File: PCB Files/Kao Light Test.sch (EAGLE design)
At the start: 12 parts, among them Q1 MMBT3904-TP

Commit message: feat: updates PCB
Adds changes from Issue #9
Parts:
- removed BT1, BT2, BT3: BHX1-1025-SM, BHX1-1025-SM:BHX1-1025-SM
- removed Q1: MMBT3904-TP, MMBT3904-TP:MMBT3904-TP
- added ANALOG: (no value), SparkFun-Connectors:JST_2MM_MALE
- added CN1: (no value), adafruit:JST_2PIN-THM
- added R10, R11, R12, R13, R14, R3, R4, R5, R6, R7, R8, R9: 1k, SparkFun-Resistors:1KOHM-HORIZ-1/4W-1%
- added T1: 2N2222, adafruit:2N2222
- R2: device SparkFun-Resistors:10KOHM-HORIZ-1/4W-1% -> SparkFun-Resistors:330OHM-HORIZ-1/10W-5%
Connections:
- removed net GND_2: DIGITAL-OUT.13, U$1.GND1
- removed net GND_3: BT3.-, DIGITAL-OUT.1
- removed net N$17: BT2.-, BT3.+
- removed net N$4: Q1.3, R2.1
- new net D14: ANALOG.+, DIGITAL-OUT.17
- net D1: now also R14.2
- net D10: now also R5.2
- net D11: now also R4.2
- net D12: now also R3.2
- net D2: now also R13.2
- net D3: now also R12.2
- net D4: now also R11.2
- net D5: now also R10.2
- net D6: now also R9.2
- net D7: now also R8.2
- net D8: now also R7.2
- net D9: now also R6.2
- net GND_1: now also ANALOG.-, CN1.1, DIGITAL-OUT.13, R10.1, R11.1, R12.1, R13.1, R14.1, R3.1, R4.1, R5.1, R6.1, R7.1, R8.1, R9.1, T1.E, U$1.GND1; no longer Q1.2
- net N$1: now also CN1.2; no longer BT1.+, U$1.VIN
- net N$2: now also R1.2, T1.B; no longer BT1.-, BT2.+
- net N$3: now also R2.1, T1.C; no longer Q1.1, R1.2

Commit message: feat: Improves the look of the PCB
Improves the naming and clenliness of the PCB
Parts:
- removed R1: 10k, SparkFun-Resistors:10KOHM-HORIZ-1/4W-1%
- removed R10, R11, R12, R3, R4, R5, R6, R7, R8, R9: 1k, SparkFun-Resistors:1KOHM-HORIZ-1/4W-1%
- removed R2: 220, SparkFun-Resistors:330OHM-HORIZ-1/10W-5%
- R13: value 1k -> 10k; device SparkFun-Resistors:1KOHM-HORIZ-1/4W-1% -> SparkFun-Resistors:10KOHM-HORIZ-1/4W-1%
- R14: value 1k -> 220; device SparkFun-Resistors:1KOHM-HORIZ-1/4W-1% -> SparkFun-Resistors:330OHM-HORIZ-1/10W-5%
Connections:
- net N$1 renamed BAT+
- net N$7 renamed 5VOUT
- removed net N$8: SERVO1.3, U$1.D11
- removed net N$9: SERVO2.3, U$1.D10
- new net PAN: SERVO1.3, U$1.D10
- new net TILT: SERVO2.3, U$1.D11
- net D1: no longer R14.2
- net D10: no longer R5.2
- net D11: no longer R4.2
- net D12: no longer R3.2
- net D13: now also R13.1; no longer R1.1
- net D2: no longer R13.2
- net D3: no longer R12.2
- net D4: no longer R11.2
- net D5: no longer R10.2
- net D6: no longer R9.2
- net D7: no longer R8.2
- net D8: no longer R7.2
- net D9: no longer R6.2
- net GND_1: no longer R10.1, R11.1, R12.1, R13.1, R14.1, R3.1, R4.1, R5.1, R6.1, R7.1, R8.1, R9.1
- net N$2: now also R13.2; no longer R1.2
- net N$3: now also R14.1; no longer R2.1
- net N$6: now also R14.2; no longer R2.2
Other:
- moved on the sheet: ANALOG, CN1, LASER, R13, R14, SERVO1, SERVO2, T1

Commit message: feat: Grounds the Cable's housing.
Also updates the images in the ReadMe
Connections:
- net GND_1: now also DIGITAL-OUT.G1, DIGITAL-OUT.G2
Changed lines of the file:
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@@
 <pinref part="U$1" gate="G$1" pin="GND1"/>
 <wire x1="101.6" y1="53.34" x2="101.6" y2="58.42" width="0.1524" layer="91"/>
-<wire x1="-12.7" y1="111.76" x2="-12.7" y2="68.58" width="0.1524" layer="91"/>
+<wire x1="-12.7" y1="111.76" x2="-12.7" y2="96.52" width="0.1524" layer="91"/>
+<wire x1="-12.7" y1="96.52" x2="-12.7" y2="68.58" width="0.1524" layer="91"/>
 <wire x1="-12.7" y1="68.58" x2="-12.7" y2="53.34" width="0.1524" layer="91"/>
-<wire x1="-12.7" y1="53.34" x2="101.6" y2="53.34" width="0.1524" layer="91"/>
+<wire x1="-12.7" y1="53.34" x2="27.94" y2="53.34" width="0.1524" layer="91"/>
 <pinref part="DIGITAL-OUT" gate="G$1" pin="13"/>
+<wire x1="27.94" y1="53.34" x2="101.6" y2="53.34" width="0.1524" layer="91"/>
 <wire x1="-5.08" y1="111.76" x2="-12.7" y2="111.76" width="0.1524" layer="91"/>
 <label x="-22.86" y="81.28" size="1.778" layer="95"/>
@@
 <junction x="81.28" y="142.24"/>
 <junction x="81.28" y="154.94"/>
+<pinref part="DIGITAL-OUT" gate="G$1" pin="G2"/>
+<wire x1="-7.62" y1="96.52" x2="-12.7" y2="96.52" width="0.1524" layer="91"/>
+<junction x="-12.7" y="96.52"/>
+<pinref part="DIGITAL-OUT" gate="G$1" pin="G1"/>
+<wire x1="27.94" y1="96.52" x2="27.94" y2="53.34" width="0.1524" layer="91"/>
+<junction x="27.94" y="53.34"/>
 </segment>
 </net>

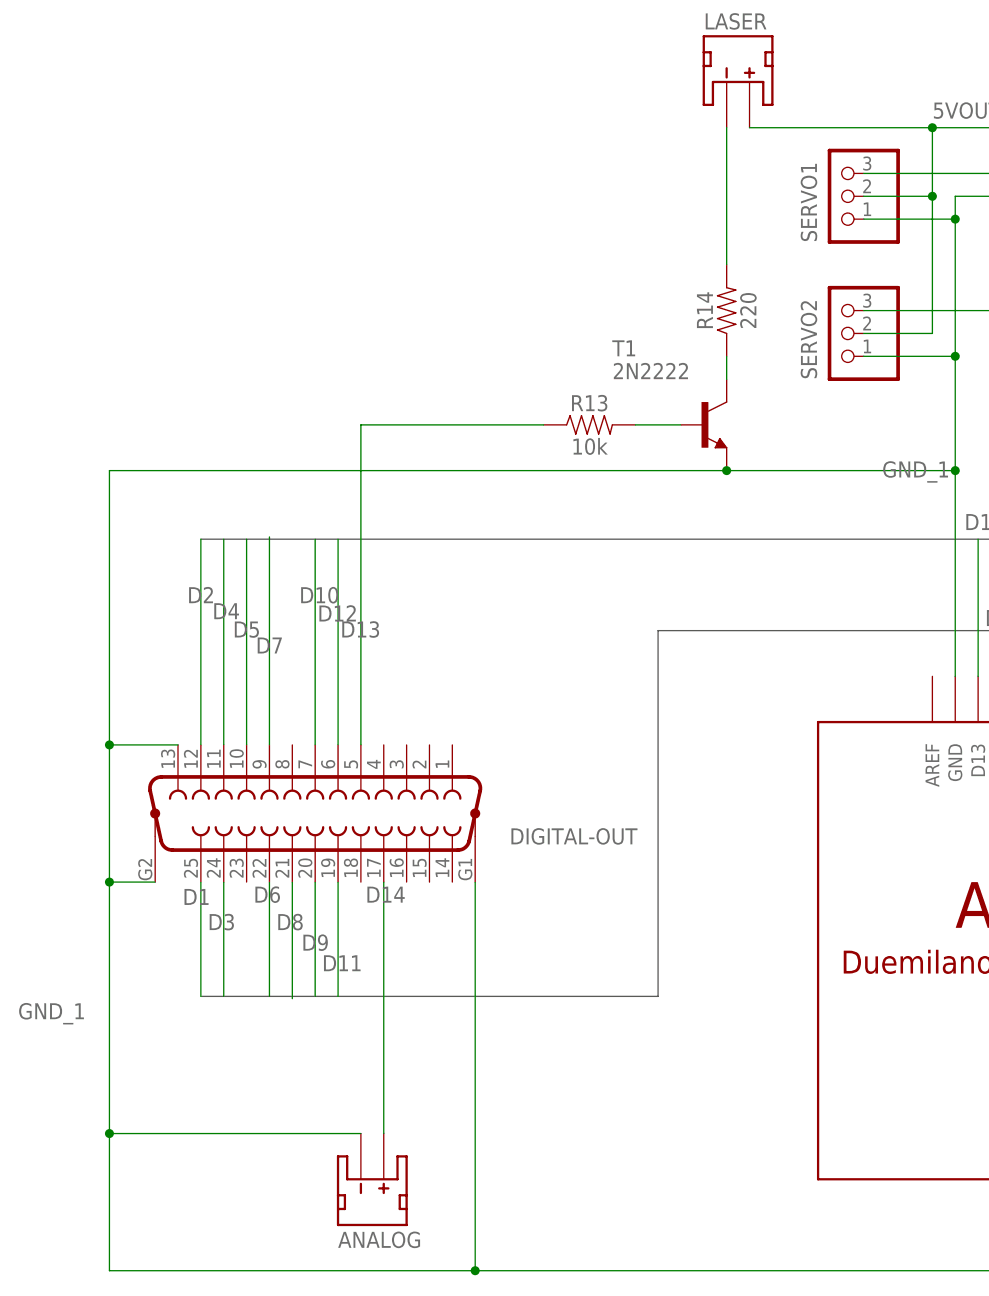
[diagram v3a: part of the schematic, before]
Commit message: docs: Updates the PCB and ReadMe to be clearer
The PCB was updated so that the servos are labeled as what they are
instead of as numbers. One resistor was also updated and all other
digital grounds were connected to the ground plane.
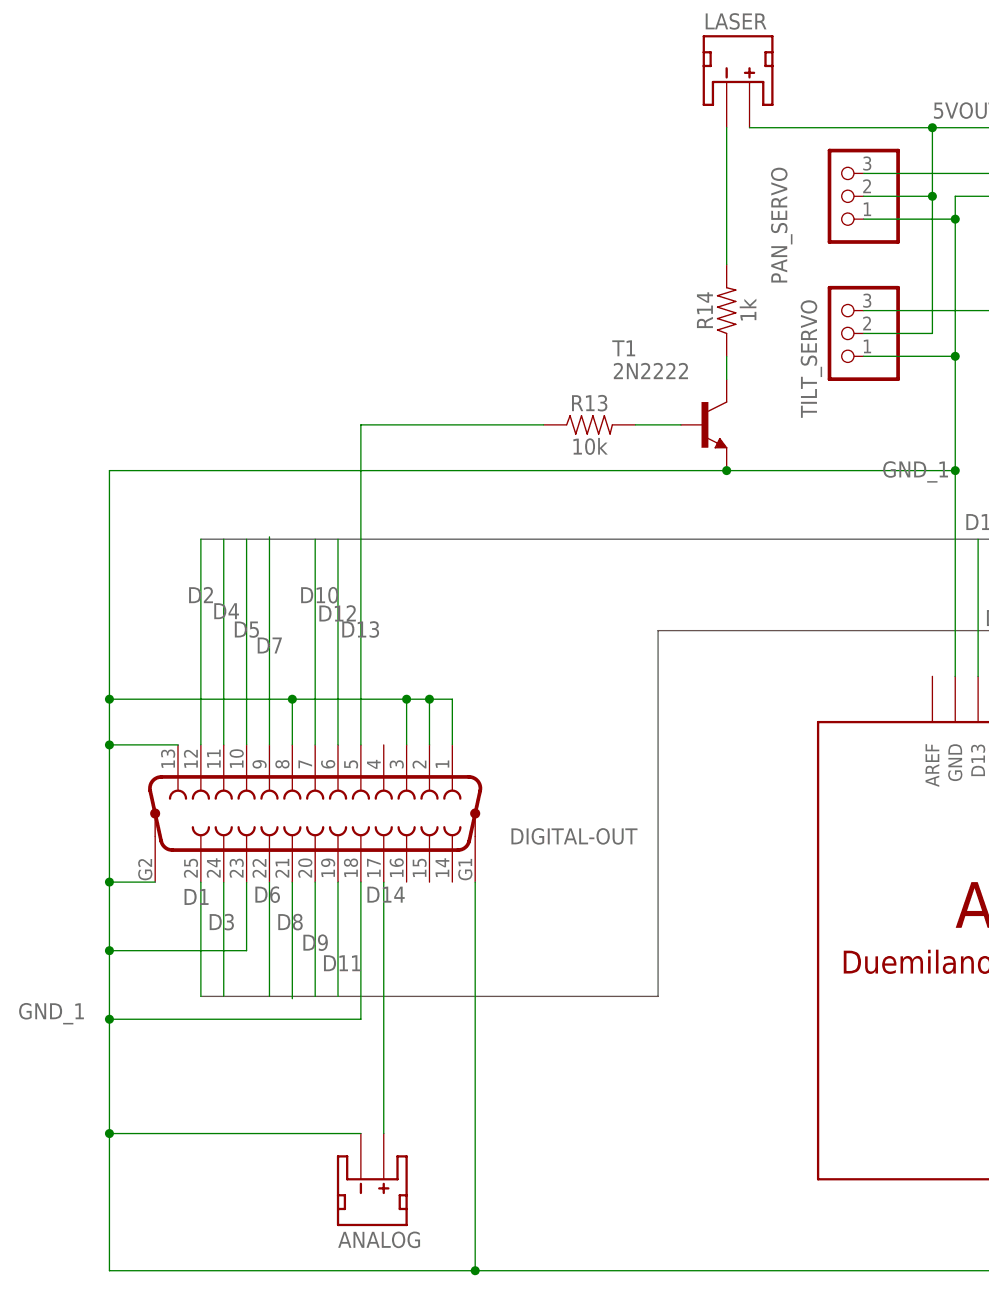
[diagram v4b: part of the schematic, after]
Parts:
- R14: value 220 -> 1k
- renumbered SERVO1 to PAN_SERVO, SERVO2 to TILT_SERVO
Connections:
- net GND_1: now also DIGITAL-OUT.1, DIGITAL-OUT.18, DIGITAL-OUT.2, DIGITAL-OUT.23, DIGITAL-OUT.3, DIGITAL-OUT.8
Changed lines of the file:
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@@
 <parts>
 <part name="LASER" library="SparkFun-Connectors" library_urn="urn:adsk.eagle:library:513" deviceset="JST_2MM_MALE" device="" package3d_urn="urn:adsk.eagle:package:38042/1"/>
-<part name="SERVO2" library="adafruit" library_urn="urn:adsk.eagle:library:420" deviceset="PINHD-1X3" device="CB" package3d_urn="urn:adsk.eagle:package:6240706/1" override_package3d_urn="urn:adsk.eagle:package:30732786/2" override_package_urn="urn:adsk.eagle:footprint:6240060/1"/>
-<part name="SERVO1" library="adafruit" library_urn="urn:adsk.eagle:library:420" deviceset="PINHD-1X3" device="CB" package3d_urn="urn:adsk.eagle:package:6240706/1" override_package3d_urn="urn:adsk.eagle:package:30732786/2" override_package_urn="urn:adsk.eagle:footprint:6240060/1"/>
+<part name="TILT_SERVO" library="adafruit" library_urn="urn:adsk.eagle:library:420" deviceset="PINHD-1X3" device="CB" package3d_urn="urn:adsk.eagle:package:6240706/1" override_package3d_urn="urn:adsk.eagle:package:30732786/2" override_package_urn="urn:adsk.eagle:footprint:6240060/1"/>
+<part name="PAN_SERVO" library="adafruit" library_urn="urn:adsk.eagle:library:420" deviceset="PINHD-1X3" device="CB" package3d_urn="urn:adsk.eagle:package:6240706/1" override_package3d_urn="urn:adsk.eagle:package:30732786/2" override_package_urn="urn:adsk.eagle:footprint:6240060/1"/>
 <part name="U$1" library="adafruit" library_urn="urn:adsk.eagle:library:420" deviceset="ARDUINO" device="UNO" package3d_urn="urn:adsk.eagle:package:6240691/1"/>
 <part name="DIGITAL-OUT" library="con-subd" library_urn="urn:adsk.eagle:library:189" deviceset="F25VP" device="" package3d_urn="urn:adsk.eagle:package:10240/1" override_package3d_urn="urn:adsk.eagle:package:30733185/2" override_package_urn="urn:adsk.eagle:footprint:10111/1"/>
@@
 <part name="CN1" library="adafruit" library_urn="urn:adsk.eagle:library:420" deviceset="JST_2PIN" device="-THM" package3d_urn="urn:adsk.eagle:package:6240693/1"/>
 <part name="R13" library="SparkFun-Resistors" library_urn="urn:adsk.eagle:library:532" deviceset="10KOHM" device="-HORIZ-1/4W-1%" package3d_urn="urn:adsk.eagle:package:39658/1" value="10k"/>
-<part name="R14" library="SparkFun-Resistors" library_urn="urn:adsk.eagle:library:532" deviceset="330OHM" device="-HORIZ-1/10W-5%" package3d_urn="urn:adsk.eagle:package:39658/1" value="220"/>
+<part name="R14" library="SparkFun-Resistors" library_urn="urn:adsk.eagle:library:532" deviceset="330OHM" device="-HORIZ-1/10W-5%" package3d_urn="urn:adsk.eagle:package:39658/1" value="1k"/>
 </parts>
 <sheets>
@@
 <attribute name="NAME" x="53.34" y="191.262" size="1.778" layer="95"/>
 </instance>
-<instance part="SERVO2" gate="A" x="68.58" y="157.48" smashed="yes" rot="R180">
+<instance part="TILT_SERVO" gate="A" x="68.58" y="157.48" smashed="yes" rot="R180">
 <attribute name="NAME" x="64.135" y="161.29" size="1.778" layer="95" rot="R270"/>
 <attribute name="VALUE" x="74.93" y="165.1" size="1.778" layer="96" rot="R180"/>
 </instance>
-<instance part="SERVO1" gate="A" x="68.58" y="172.72" smashed="yes" rot="R180">
-<attribute name="NAME" x="64.135" y="176.53" size="1.778" layer="95" rot="R270"/>
+<instance part="PAN_SERVO" gate="A" x="68.58" y="172.72" smashed="yes" rot="R180">
+<attribute name="NAME" x="60.833" y="176.022" size="1.778" layer="95" rot="R270"/>
 <attribute name="VALUE" x="74.93" y="180.34" size="1.778" layer="96" rot="R180"/>
 </instance>
@@
 <net name="TILT" class="0">
 <segment>
-<pinref part="SERVO2" gate="A" pin="3"/>
+<pinref part="TILT_SERVO" gate="A" pin="3"/>
 <wire x1="71.12" y1="160.02" x2="88.9" y2="160.02" width="0.1524" layer="91"/>
 <pinref part="U$1" gate="G$1" pin="D11"/>
@@
 <pinref part="U$1" gate="G$1" pin="D10"/>
 <wire x1="91.44" y1="119.38" x2="91.44" y2="175.26" width="0.1524" layer="91"/>
-<pinref part="SERVO1" gate="A" pin="3"/>
+<pinref part="PAN_SERVO" gate="A" pin="3"/>
 <wire x1="91.44" y1="175.26" x2="71.12" y2="175.26" width="0.1524" layer="91"/>
 <label x="88.9" y="165.1" size="1.778" layer="95"/>
@@
 <wire x1="101.6" y1="53.34" x2="101.6" y2="58.42" width="0.1524" layer="91"/>
 <wire x1="-12.7" y1="111.76" x2="-12.7" y2="96.52" width="0.1524" layer="91"/>
-<wire x1="-12.7" y1="96.52" x2="-12.7" y2="68.58" width="0.1524" layer="91"/>
+<wire x1="-12.7" y1="96.52" x2="-12.7" y2="88.9" width="0.1524" layer="91"/>
+<wire x1="-12.7" y1="88.9" x2="-12.7" y2="81.28" width="0.1524" layer="91"/>
+<wire x1="-12.7" y1="81.28" x2="-12.7" y2="68.58" width="0.1524" layer="91"/>
 <wire x1="-12.7" y1="68.58" x2="-12.7" y2="53.34" width="0.1524" layer="91"/>
 <wire x1="-12.7" y1="53.34" x2="27.94" y2="53.34" width="0.1524" layer="91"/>
@@
 <wire x1="81.28" y1="142.24" x2="55.88" y2="142.24" width="0.1524" layer="91"/>
 <label x="73.152" y="141.478" size="1.778" layer="95"/>
-<wire x1="-12.7" y1="111.76" x2="-12.7" y2="142.24" width="0.1524" layer="91"/>
+<wire x1="-12.7" y1="111.76" x2="-12.7" y2="116.84" width="0.1524" layer="91"/>
+<wire x1="-12.7" y1="116.84" x2="-12.7" y2="142.24" width="0.1524" layer="91"/>
 <wire x1="-12.7" y1="142.24" x2="55.88" y2="142.24" width="0.1524" layer="91"/>
 <junction x="-12.7" y="111.76"/>
@@
 <pinref part="5V_REG" gate="A" pin="COMMON"/>
 <wire x1="96.52" y1="172.72" x2="81.28" y2="172.72" width="0.1524" layer="91"/>
-<pinref part="SERVO2" gate="A" pin="1"/>
+<pinref part="TILT_SERVO" gate="A" pin="1"/>
 <wire x1="71.12" y1="154.94" x2="81.28" y2="154.94" width="0.1524" layer="91"/>
-<pinref part="SERVO1" gate="A" pin="1"/>
+<pinref part="PAN_SERVO" gate="A" pin="1"/>
 <wire x1="81.28" y1="154.94" x2="81.28" y2="170.18" width="0.1524" layer="91"/>
 <wire x1="81.28" y1="170.18" x2="71.12" y2="170.18" width="0.1524" layer="91"/>
@@
 <wire x1="27.94" y1="96.52" x2="27.94" y2="53.34" width="0.1524" layer="91"/>
 <junction x="27.94" y="53.34"/>
+<pinref part="DIGITAL-OUT" gate="G$1" pin="23"/>
+<wire x1="2.54" y1="96.52" x2="2.54" y2="88.9" width="0.1524" layer="91"/>
+<wire x1="2.54" y1="88.9" x2="-12.7" y2="88.9" width="0.1524" layer="91"/>
+<junction x="-12.7" y="88.9"/>
+<pinref part="DIGITAL-OUT" gate="G$1" pin="8"/>
+<wire x1="7.62" y1="111.76" x2="7.62" y2="116.84" width="0.1524" layer="91"/>
+<wire x1="7.62" y1="116.84" x2="-12.7" y2="116.84" width="0.1524" layer="91"/>
+<junction x="-12.7" y="116.84"/>
+<pinref part="DIGITAL-OUT" gate="G$1" pin="18"/>
+<wire x1="15.24" y1="96.52" x2="15.24" y2="81.28" width="0.1524" layer="91"/>
+<wire x1="15.24" y1="81.28" x2="-12.7" y2="81.28" width="0.1524" layer="91"/>
+<junction x="-12.7" y="81.28"/>
+<pinref part="DIGITAL-OUT" gate="G$1" pin="3"/>
+<wire x1="20.32" y1="111.76" x2="20.32" y2="116.84" width="0.1524" layer="91"/>
+<wire x1="20.32" y1="116.84" x2="7.62" y2="116.84" width="0.1524" layer="91"/>
+<junction x="7.62" y="116.84"/>
+<pinref part="DIGITAL-OUT" gate="G$1" pin="2"/>
+<wire x1="22.86" y1="111.76" x2="22.86" y2="116.84" width="0.1524" layer="91"/>
+<wire x1="22.86" y1="116.84" x2="20.32" y2="116.84" width="0.1524" layer="91"/>
+<junction x="20.32" y="116.84"/>
+<pinref part="DIGITAL-OUT" gate="G$1" pin="1"/>
+<wire x1="25.4" y1="111.76" x2="25.4" y2="116.84" width="0.1524" layer="91"/>
+<wire x1="25.4" y1="116.84" x2="22.86" y2="116.84" width="0.1524" layer="91"/>
+<junction x="22.86" y="116.84"/>
 </segment>
 </net>
@@
 <net name="5VOUT" class="0">
 <segment>
-<pinref part="SERVO2" gate="A" pin="2"/>
+<pinref part="TILT_SERVO" gate="A" pin="2"/>
 <wire x1="71.12" y1="157.48" x2="78.74" y2="157.48" width="0.1524" layer="91"/>
 <wire x1="78.74" y1="157.48" x2="78.74" y2="172.72" width="0.1524" layer="91"/>
-<pinref part="SERVO1" gate="A" pin="2"/>
+<pinref part="PAN_SERVO" gate="A" pin="2"/>
 <wire x1="78.74" y1="172.72" x2="71.12" y2="172.72" width="0.1524" layer="91"/>
 <pinref part="5V_REG" gate="A" pin="OUTPUT"/>
